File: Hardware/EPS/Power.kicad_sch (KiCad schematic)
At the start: 15 parts

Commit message: EPS v0.0.1
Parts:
- added C?: 10u, symbol Device:C
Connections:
- net EN_3V3: no longer U?.4 (EN)
- net GND: now also C?.2
- net VBUS_IN: now also C?.1
- new net EN_5V0: U?.4 (EN)
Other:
- note added: "Add tps270 to control switching of 3.3V rail"

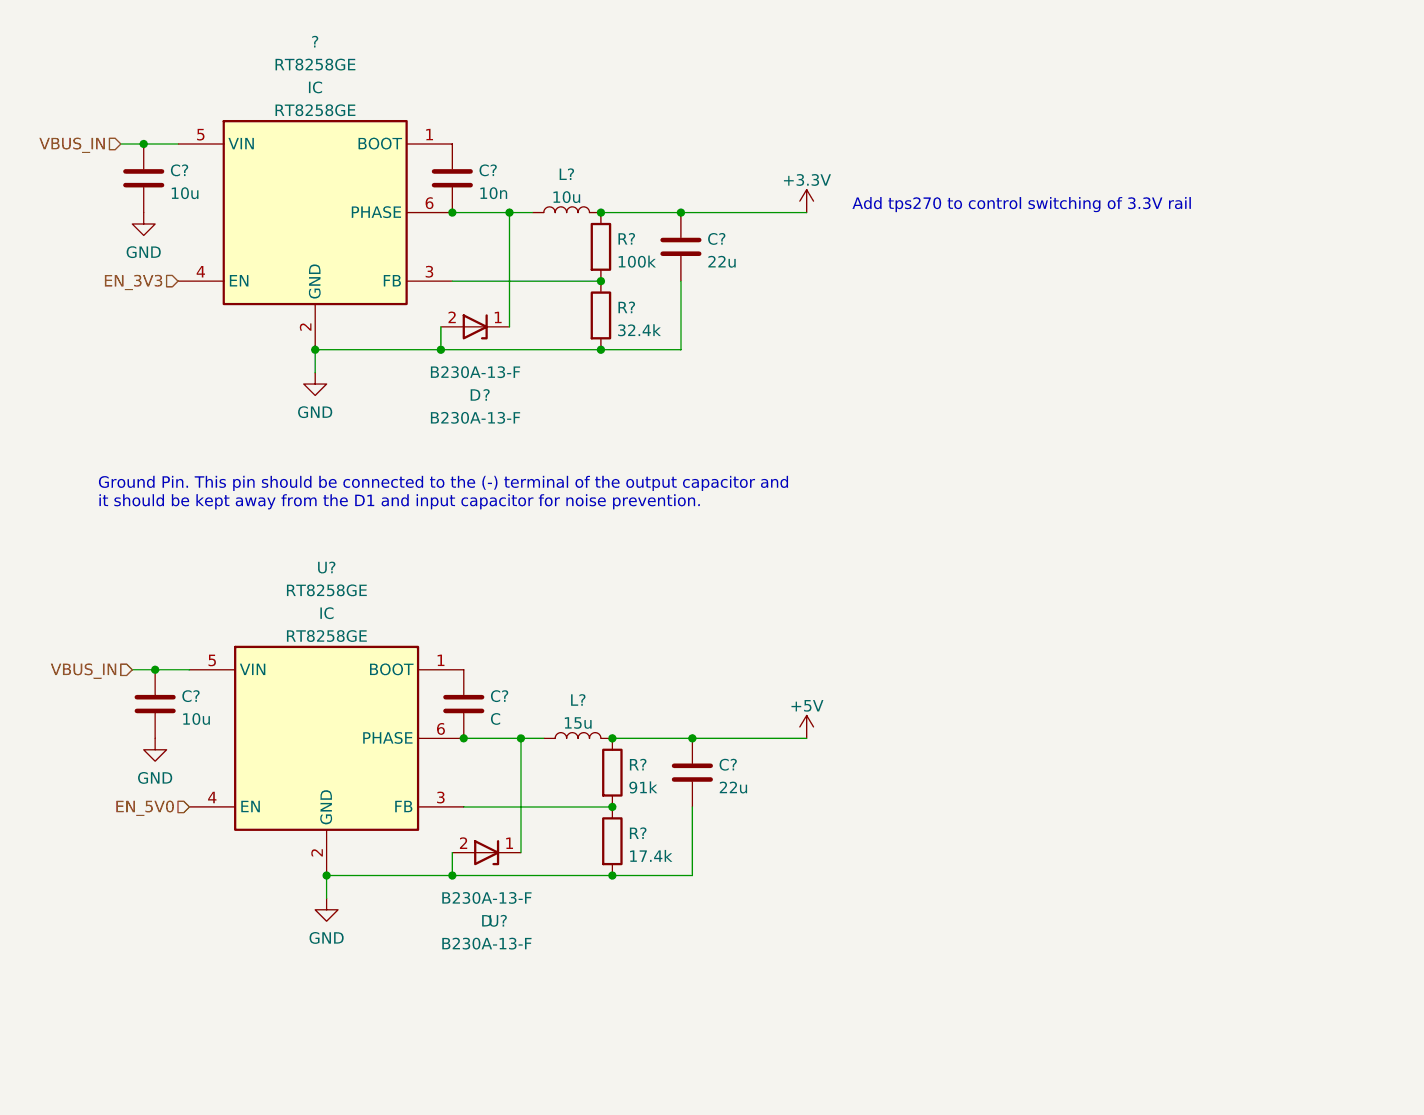
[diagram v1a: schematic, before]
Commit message: Fuse, Power Switch to 3.3V, connector ESD Prot.
v0.0.2
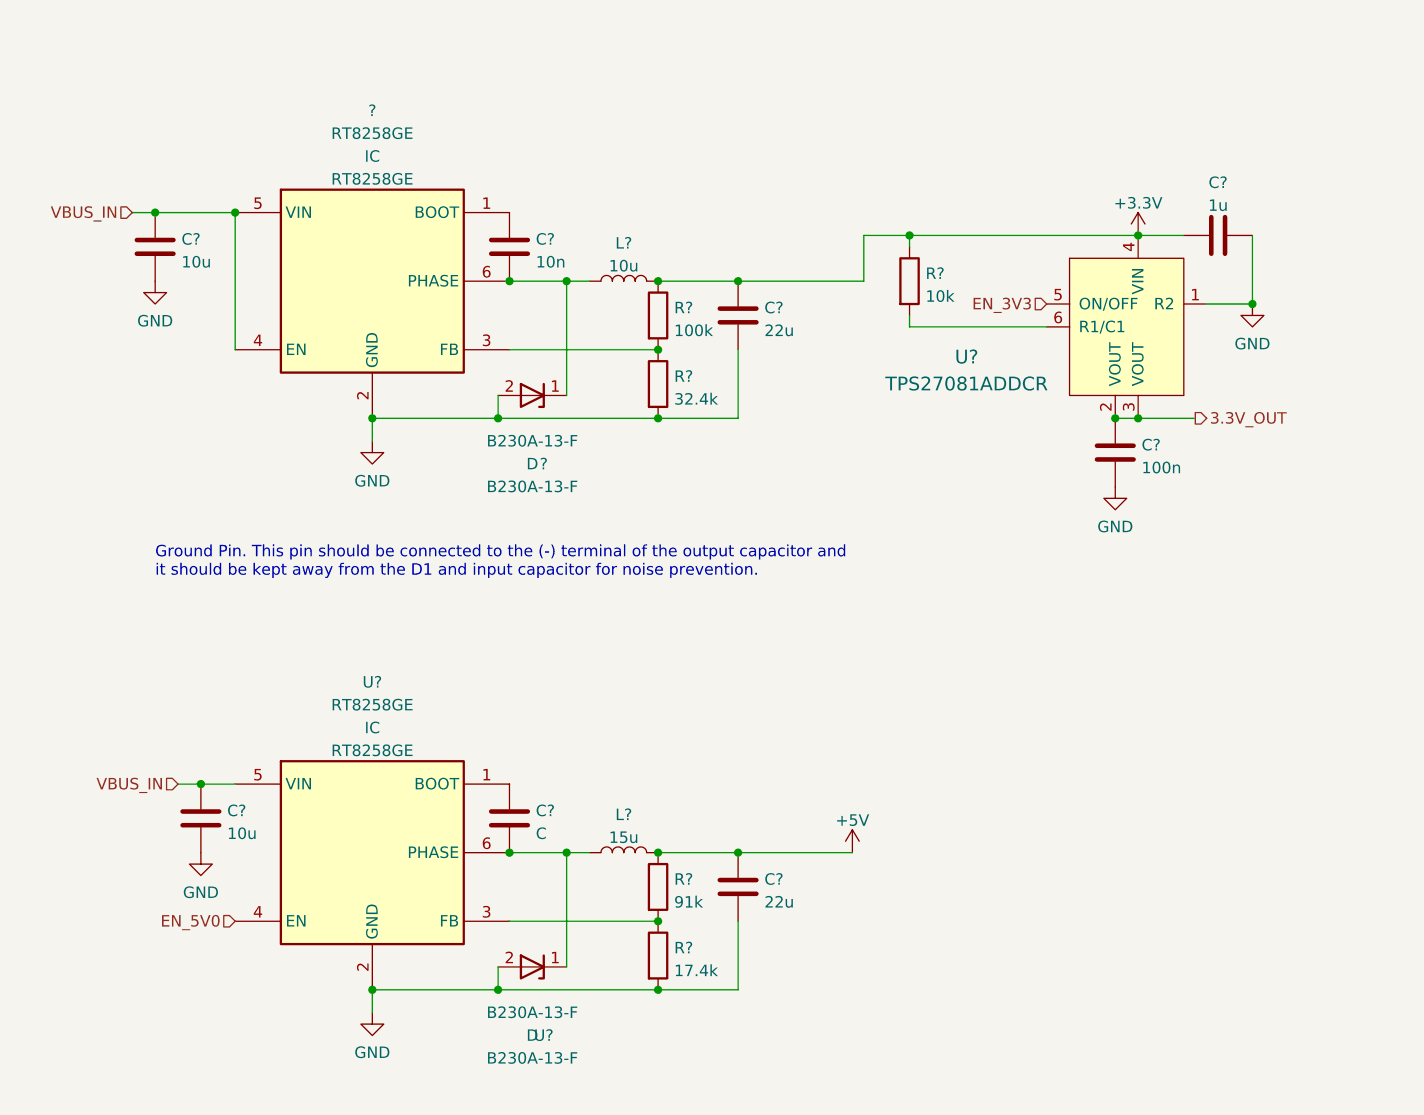
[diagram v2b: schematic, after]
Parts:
- added C?: 100n, symbol Device:C
- added C?: 1u, symbol Device:C
- added R?: 10k, symbol Device:R
- added U?: TPS27081ADDCR, digikey-footprints:SOT-23-6, symbol dk_PMIC-Power-Distribution-Switches-Load-Drivers:TPS27081ADDCR
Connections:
- net +3.3V: now also C?.2, R?.1, U?.4 (VIN)
- net EN_3V3: now also U?.5 (ON/OFF); no longer ?.4 (EN)
- net GND: now also C?.1, C?.2, U?.1 (R2)
- net VBUS_IN: now also ?.4 (EN)
- new net: R?.2, U?.6 (R1/C1)
- new net 3.3V_OUT: C?.1, U?.2 (VOUT), U?.3 (VOUT)
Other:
- note removed: "Add tps270 to control switching of 3.3V rail"
- title: (none) -> EPS Schematics
- moved on the sheet: ?, C?, L?, R?, U?

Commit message: Reworked LTC4162 Symbol
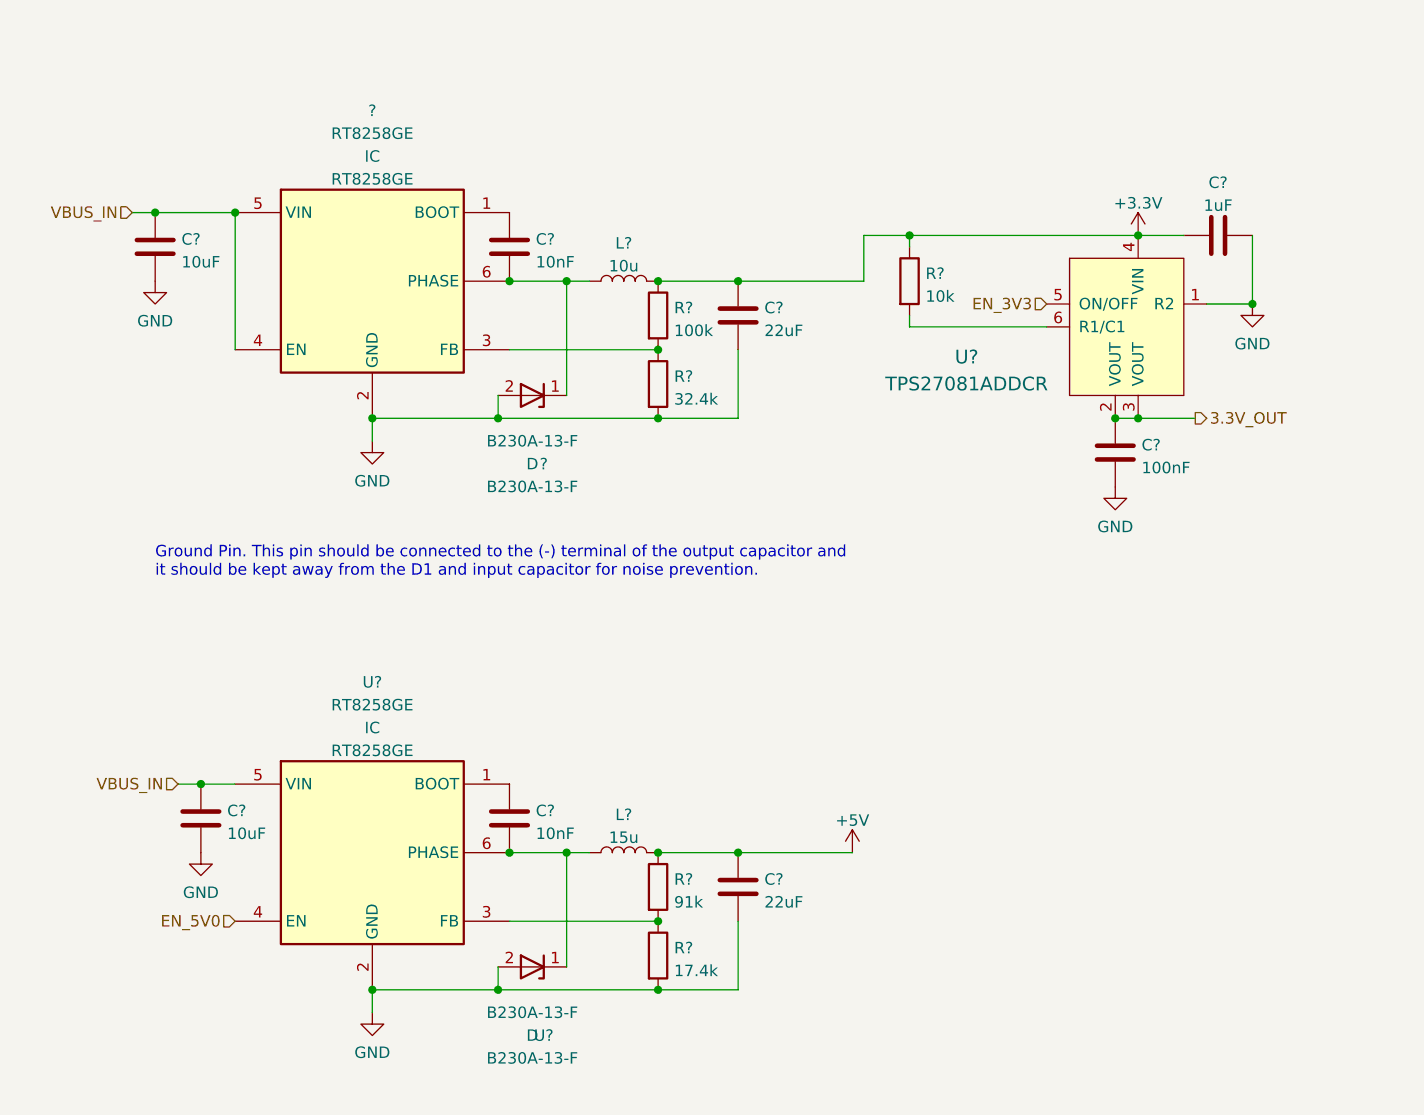
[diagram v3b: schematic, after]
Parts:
- C?: value C -> 10nF
- C? (x2): value 22u -> 22uF
- C?: value 100n -> 100nF
- C?: value 1u -> 1uF
- C? (x2): value 10u -> 10uF
- C?: value 10n -> 10nF
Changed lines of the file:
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@@
     )
   )
-  (image (at 255.27 30.48) (scale 0.822046)
+  (image (at 248.92 34.29) (scale 1.00048)
     (data
       iVBORw0KGgoAAAANSUhEUgAAA1IAAAIACAIAAAAHdcoYAAAAA3NCSVQICAjb4U/gAAAgAElEQVR4
@@
       (effects (font (size 1.27 1.27)) (justify left))
     )
-    (property "Value" "C" (id 1) (at 150.241 131.2422 0)
+    (property "Value" "10nF" (id 1) (at 150.241 131.2422 0)
       (effects (font (size 1.27 1.27)) (justify left))
     )
@@
       (effects (font (size 1.27 1.27)) (justify left))
     )
-    (property "Value" "22u" (id 1) (at 175.641 75.3622 0)
+    (property "Value" "22uF" (id 1) (at 175.641 75.3622 0)
       (effects (font (size 1.27 1.27)) (justify left))
     )
@@
       (effects (font (size 1.27 1.27)) (justify left))
     )
-    (property "Value" "100n" (id 1) (at 217.551 90.6022 0)
+    (property "Value" "100nF" (id 1) (at 217.551 90.6022 0)
       (effects (font (size 1.27 1.27)) (justify left))
     )
@@
     (in_bom yes) (on_board yes) (fields_autoplaced)
     (property "Reference" "C?" (id 0) (at 226.06 58.9112 90))
-    (property "Value" "1u" (id 1) (at 226.06 61.4481 90))
+    (property "Value" "1uF" (id 1) (at 226.06 61.4481 90))
     (property "Footprint" "" (id 2) (at 222.25 65.7352 0)
       (effects (font (size 1.27 1.27)) hide)
@@
       (effects (font (size 1.27 1.27)) (justify left))
     )
-    (property "Value" "10u" (id 1) (at 115.951 131.2422 0)
+    (property "Value" "10uF" (id 1) (at 115.951 131.2422 0)
       (effects (font (size 1.27 1.27)) (justify left))
     )
@@
       (effects (font (size 1.27 1.27)) (justify left))
     )
-    (property "Value" "10u" (id 1) (at 110.871 67.7422 0)
+    (property "Value" "10uF" (id 1) (at 110.871 67.7422 0)
       (effects (font (size 1.27 1.27)) (justify left))
     )
@@
       (effects (font (size 1.27 1.27)) (justify left))
     )
-    (property "Value" "10n" (id 1) (at 150.241 67.7422 0)
+    (property "Value" "10nF" (id 1) (at 150.241 67.7422 0)
       (effects (font (size 1.27 1.27)) (justify left))
     )
@@
       (effects (font (size 1.27 1.27)) (justify left))
     )
-    (property "Value" "22u" (id 1) (at 175.641 138.8622 0)
-      (effects (font (size 1.27 1.27)) (justify left))
-    )
+    (property "Value" "22uF" (id 1) (at 175.641 138.8622 0)
+      (effects (font (size 1.27 1.27)) (justify left))
+    )

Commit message: Defined pinout for board connector, major revision
v0.0.3 - Fixed erratas and cleaned the schematic
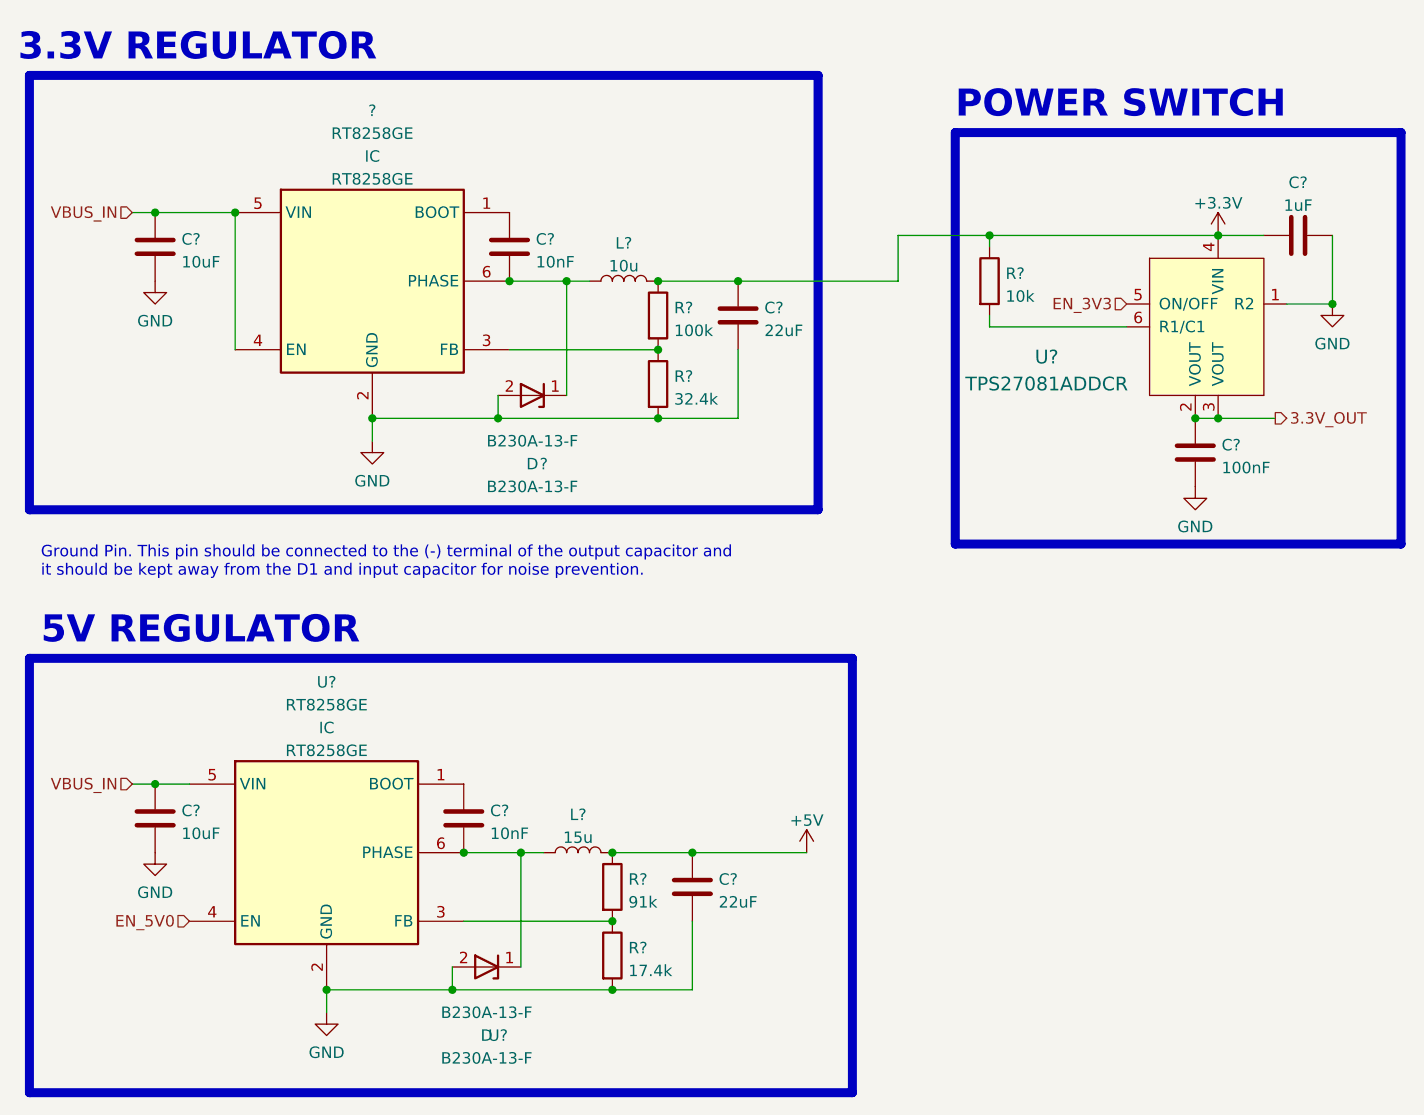
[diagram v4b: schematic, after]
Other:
- note added: "3.3V REGULATOR"
- note added: "5V REGULATOR"
- note added: "POWER SWITCH"
- moved on the sheet: C?, L?, R?, U?
